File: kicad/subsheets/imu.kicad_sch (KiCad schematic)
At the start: 5 parts

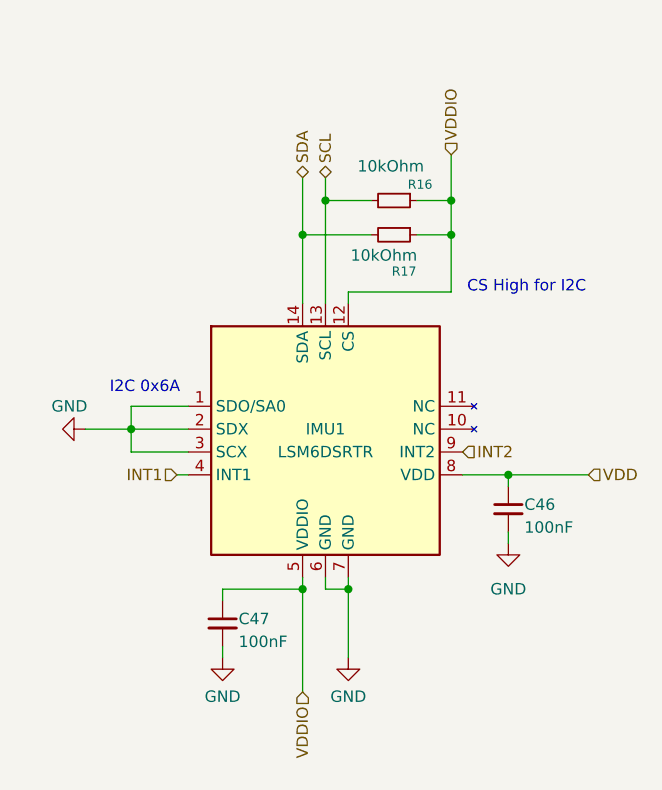
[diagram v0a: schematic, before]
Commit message: Clean up IMU wiring
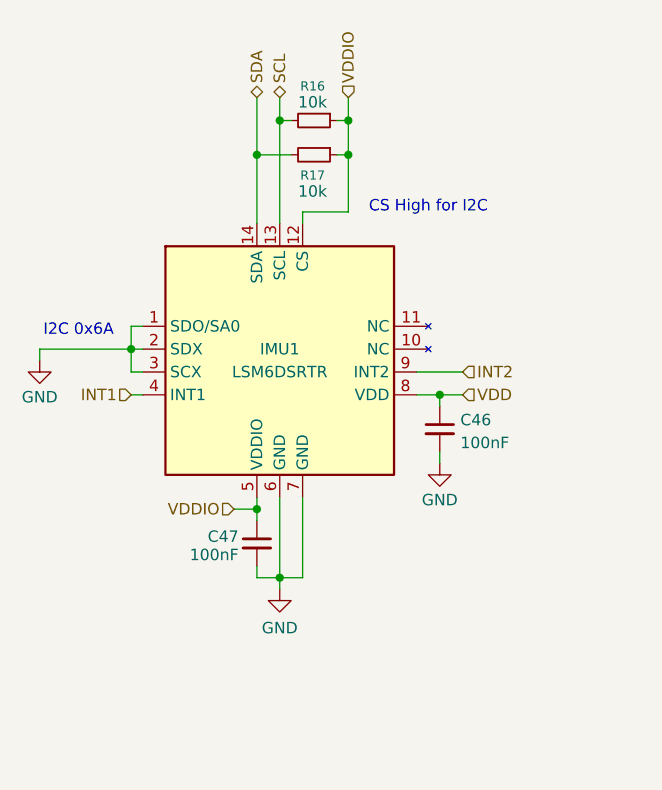
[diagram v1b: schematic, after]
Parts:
- R16, R17: value 10kOhm -> 10k
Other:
- moved on the sheet: C46, C47, IMU1, R16, R17

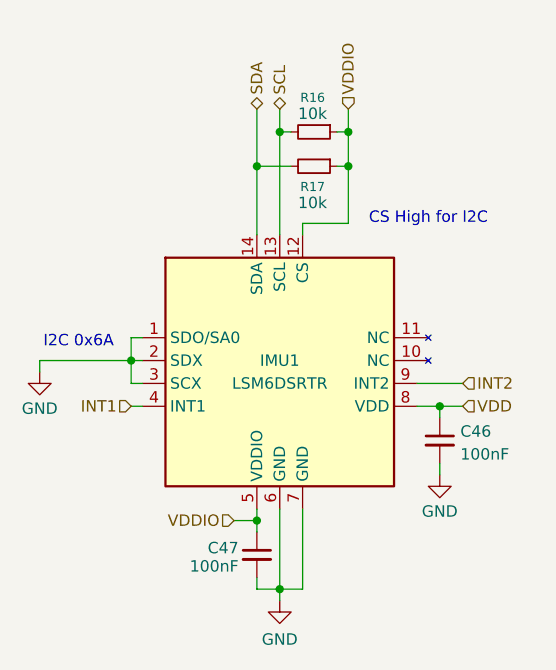
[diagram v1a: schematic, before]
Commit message: Wire peripherals to STM
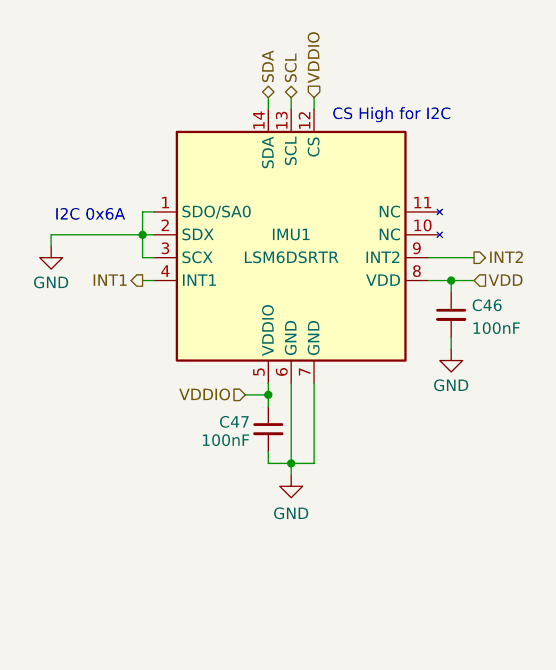
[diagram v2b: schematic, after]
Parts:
- removed R16, R17: 10k, symbol Device:R_Small
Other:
- moved on the sheet: C46, C47, IMU1

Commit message: Minor changes
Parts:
- renumbered C46 to C50, C47 to C51
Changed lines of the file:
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@@
 		(on_board yes)
 		(dnp no)
-		(property "Reference" "C47"
+		(property "Reference" "C51"
 			(at 62.738 60.198 0)
 			(effects
@@
 			(project "srad-camera"
 				(path "/da62c771-e8c9-451f-8df1-ec995aadcb11/53c61148-5ca8-449f-9011-3672d8a04f56"
-					(reference "C47")
+					(reference "C51")
 					(unit 1)
 				)
@@
 		(on_board yes)
 		(dnp no)
-		(property "Reference" "#PWR025"
+		(property "Reference" "#PWR022"
 			(at 40.64 46.99 0)
 			(effects
@@
 			(project "srad-camera"
 				(path "/da62c771-e8c9-451f-8df1-ec995aadcb11/53c61148-5ca8-449f-9011-3672d8a04f56"
-					(reference "#PWR025")
+					(reference "#PWR022")
 					(unit 1)
 				)
@@
 		(on_board yes)
 		(dnp no)
-		(property "Reference" "#PWR026"
+		(property "Reference" "#PWR023"
 			(at 85.09 58.42 0)
 			(effects
@@
 			(project "srad-camera"
 				(path "/da62c771-e8c9-451f-8df1-ec995aadcb11/53c61148-5ca8-449f-9011-3672d8a04f56"
-					(reference "#PWR026")
+					(reference "#PWR023")
 					(unit 1)
 				)
@@
 		(on_board yes)
 		(dnp no)
-		(property "Reference" "C46"
+		(property "Reference" "C50"
 			(at 87.376 47.244 0)
 			(effects
@@
 			(project "srad-camera"
 				(path "/da62c771-e8c9-451f-8df1-ec995aadcb11/53c61148-5ca8-449f-9011-3672d8a04f56"
-					(reference "C46")
+					(reference "C50")
 					(unit 1)
 				)
@@
 		(on_board yes)
 		(dnp no)
-		(property "Reference" "#PWR028"
+		(property "Reference" "#PWR024"
 			(at 67.31 72.39 0)
 			(effects
@@
 			(project "srad-camera"
 				(path "/da62c771-e8c9-451f-8df1-ec995aadcb11/53c61148-5ca8-449f-9011-3672d8a04f56"
-					(reference "#PWR028")
-					(unit 1)
-				)
+					(reference "#PWR024")
+					(unit 1)
+				)

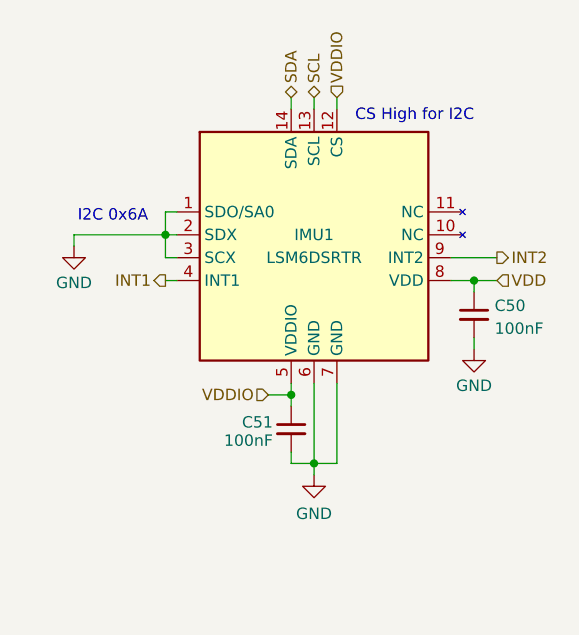
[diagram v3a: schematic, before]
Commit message: Make sure logic levels are correct between ICs
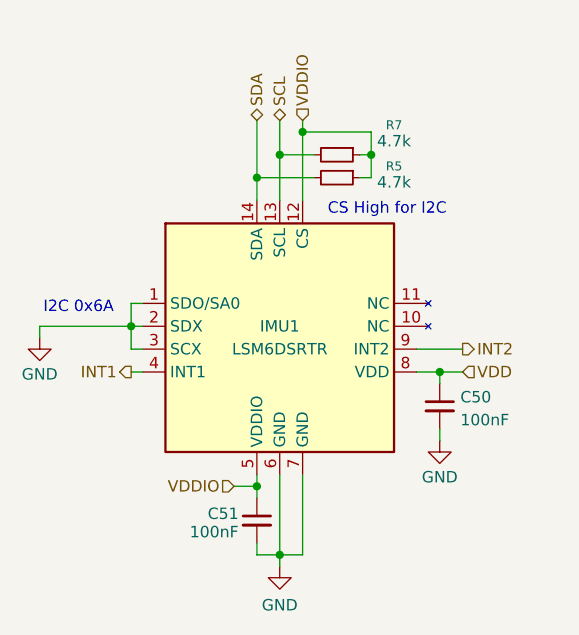
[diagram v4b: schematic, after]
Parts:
- added R5, R7: 4.7k, symbol Device:R_Small
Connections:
- net SCL: now also R7.2
- net SDA: now also R5.2
- net VDDIO: now also R5.1, R7.1
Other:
- moved on the sheet: C50, C51, IMU1

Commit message: Annotations
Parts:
- renumbered C50 to C53, C51 to C54, R7 to R28, R5 to R29
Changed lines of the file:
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@@
 		(on_board yes)
 		(dnp no)
-		(property "Reference" "R7"
+		(property "Reference" "R28"
 			(at 76.2 27.178 90)
 			(effects
@@
 			(project "srad-camera"
 				(path "/da62c771-e8c9-451f-8df1-ec995aadcb11/53c61148-5ca8-449f-9011-3672d8a04f56"
-					(reference "R7")
+					(reference "R28")
 					(unit 1)
 				)
@@
 		(on_board yes)
 		(dnp no)
-		(property "Reference" "C51"
+		(property "Reference" "C54"
 			(at 58.928 70.358 0)
 			(effects
@@
 			(project "srad-camera"
 				(path "/da62c771-e8c9-451f-8df1-ec995aadcb11/53c61148-5ca8-449f-9011-3672d8a04f56"
-					(reference "C51")
+					(reference "C54")
 					(unit 1)
 				)
@@
 		(on_board yes)
 		(dnp no)
-		(property "Reference" "#PWR022"
+		(property "Reference" "#PWR033"
 			(at 36.83 57.15 0)
 			(effects
@@
 			(project "srad-camera"
 				(path "/da62c771-e8c9-451f-8df1-ec995aadcb11/53c61148-5ca8-449f-9011-3672d8a04f56"
-					(reference "#PWR022")
+					(reference "#PWR033")
 					(unit 1)
 				)
@@
 		(on_board yes)
 		(dnp no)
-		(property "Reference" "#PWR023"
+		(property "Reference" "#PWR034"
 			(at 81.28 68.58 0)
 			(effects
@@
 			(project "srad-camera"
 				(path "/da62c771-e8c9-451f-8df1-ec995aadcb11/53c61148-5ca8-449f-9011-3672d8a04f56"
-					(reference "#PWR023")
+					(reference "#PWR034")
 					(unit 1)
 				)
@@
 		(on_board yes)
 		(dnp no)
-		(property "Reference" "C50"
+		(property "Reference" "C53"
 			(at 83.566 57.404 0)
 			(effects
@@
 			(project "srad-camera"
 				(path "/da62c771-e8c9-451f-8df1-ec995aadcb11/53c61148-5ca8-449f-9011-3672d8a04f56"
-					(reference "C50")
+					(reference "C53")
 					(unit 1)
 				)
@@
 		(on_board yes)
 		(dnp no)
-		(property "Reference" "#PWR024"
+		(property "Reference" "#PWR035"
 			(at 63.5 82.55 0)
 			(effects
@@
 			(project "srad-camera"
 				(path "/da62c771-e8c9-451f-8df1-ec995aadcb11/53c61148-5ca8-449f-9011-3672d8a04f56"
-					(reference "#PWR024")
+					(reference "#PWR035")
 					(unit 1)
 				)
@@
 		(on_board yes)
 		(dnp no)
-		(property "Reference" "R5"
+		(property "Reference" "R29"
 			(at 76.2 31.75 90)
 			(effects
@@
 			(project "srad-camera"
 				(path "/da62c771-e8c9-451f-8df1-ec995aadcb11/53c61148-5ca8-449f-9011-3672d8a04f56"
-					(reference "R5")
-					(unit 1)
-				)
+					(reference "R29")
+					(unit 1)
+				)

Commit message: Annotations + minor tweaks
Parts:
- renumbered C53 to C50, C54 to C51, R28 to R27, R29 to R28

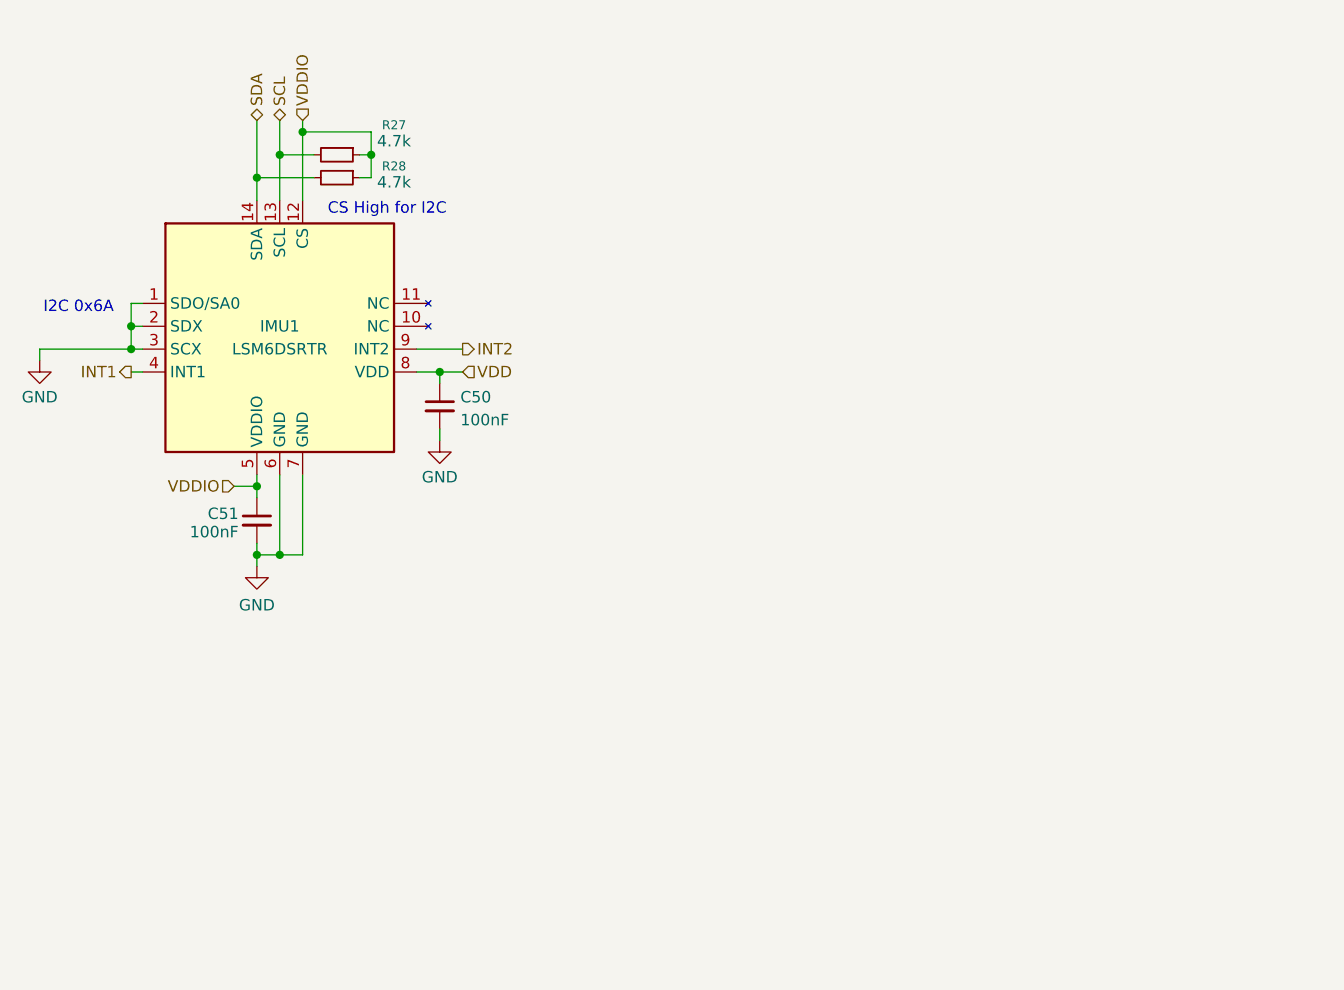
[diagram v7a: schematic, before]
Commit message: Change all sheets to A4, name sheets, split RK3566 into hierarchy
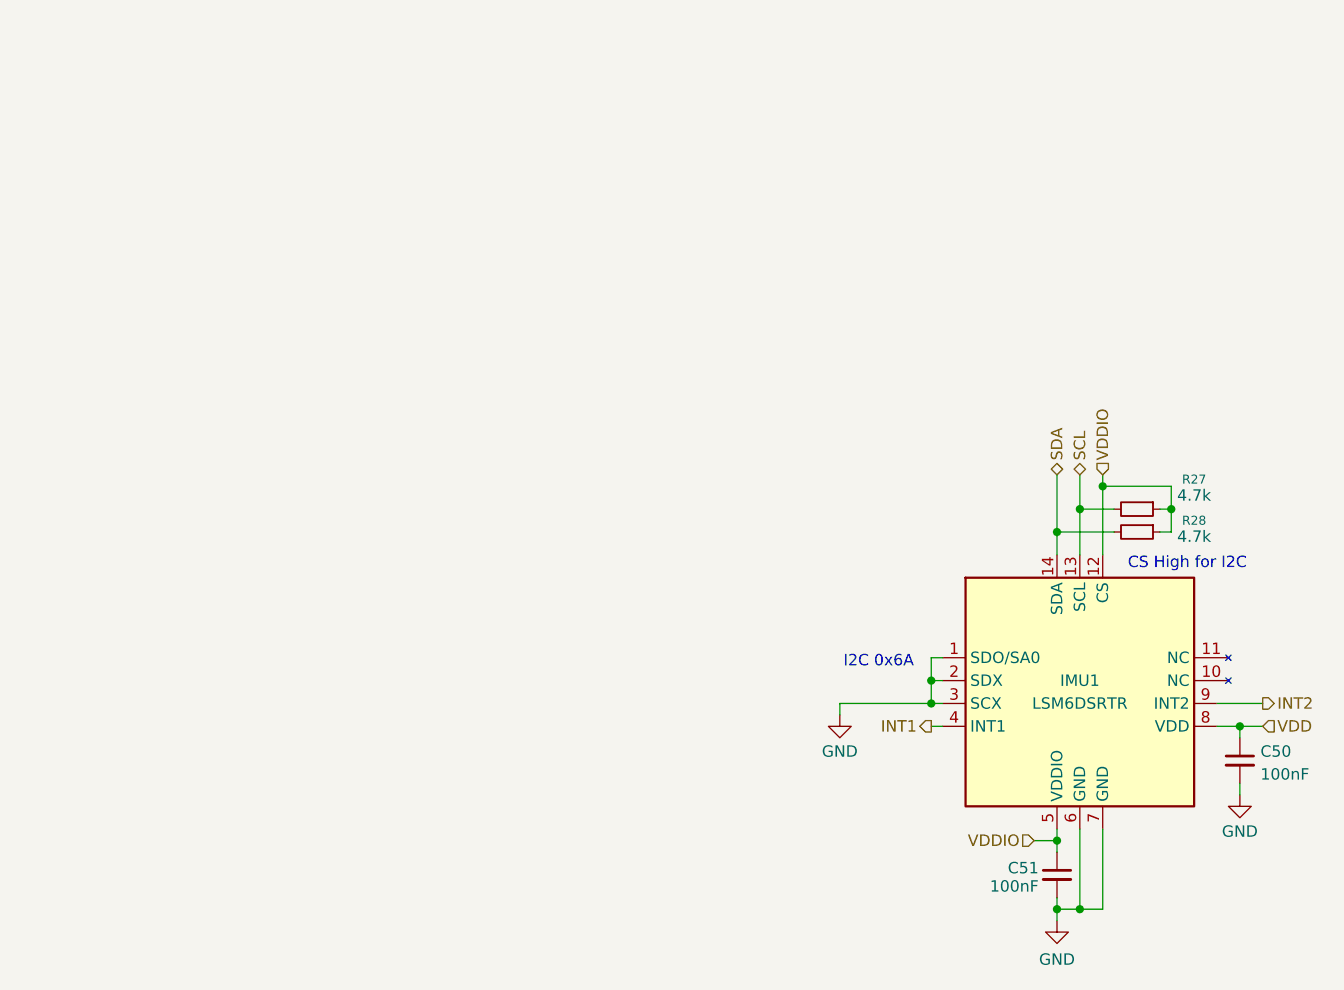
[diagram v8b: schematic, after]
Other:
- title: (none) -> Inertial Measurement Unit
- moved on the sheet: C50, C51, IMU1, R27, R28
